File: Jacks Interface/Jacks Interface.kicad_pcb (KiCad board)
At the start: 2 copper layers, 100.6 x 33.7 mm, 11 parts, among them J1 INPUT, J10 EARTH, J11 RETURN, J2 To board GND, J3 To board IN, J4 From battery minus, J5 To board OUT, J6 OUTPUT, J7 SEND, J8 To board SEND, J9 To board RETURN

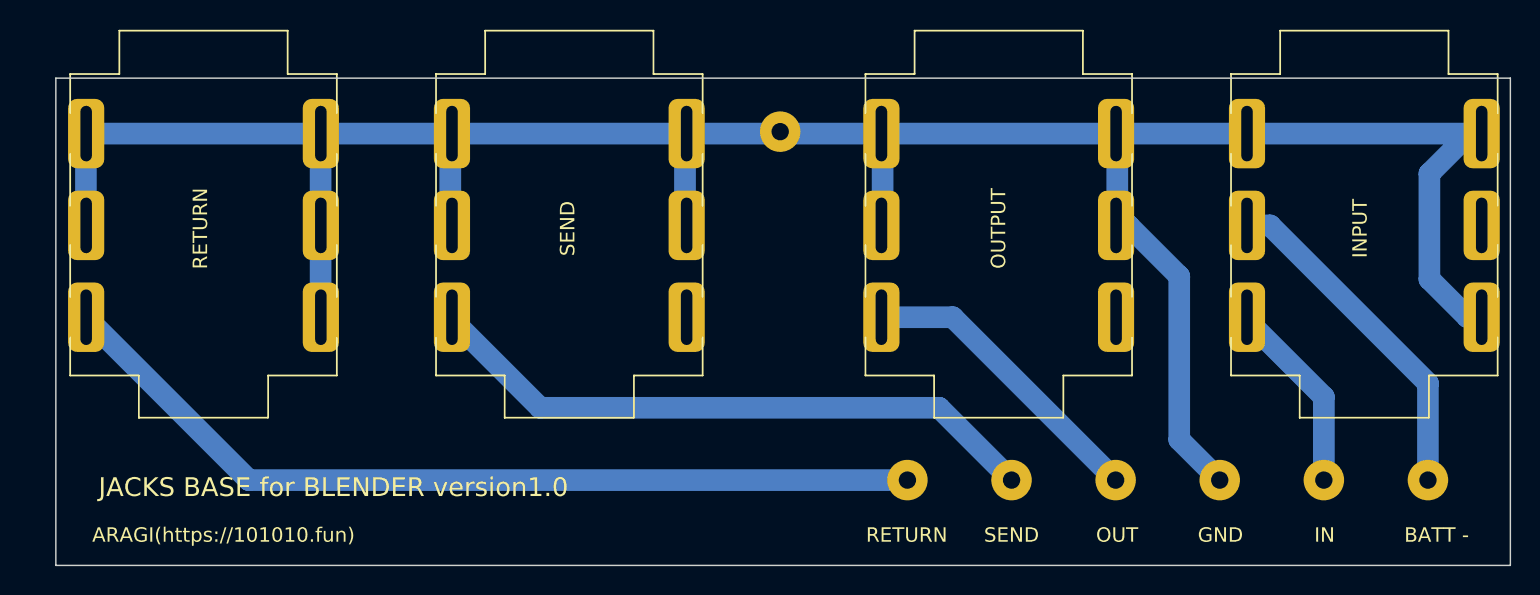
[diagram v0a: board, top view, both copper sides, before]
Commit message: fix: 回路の修正
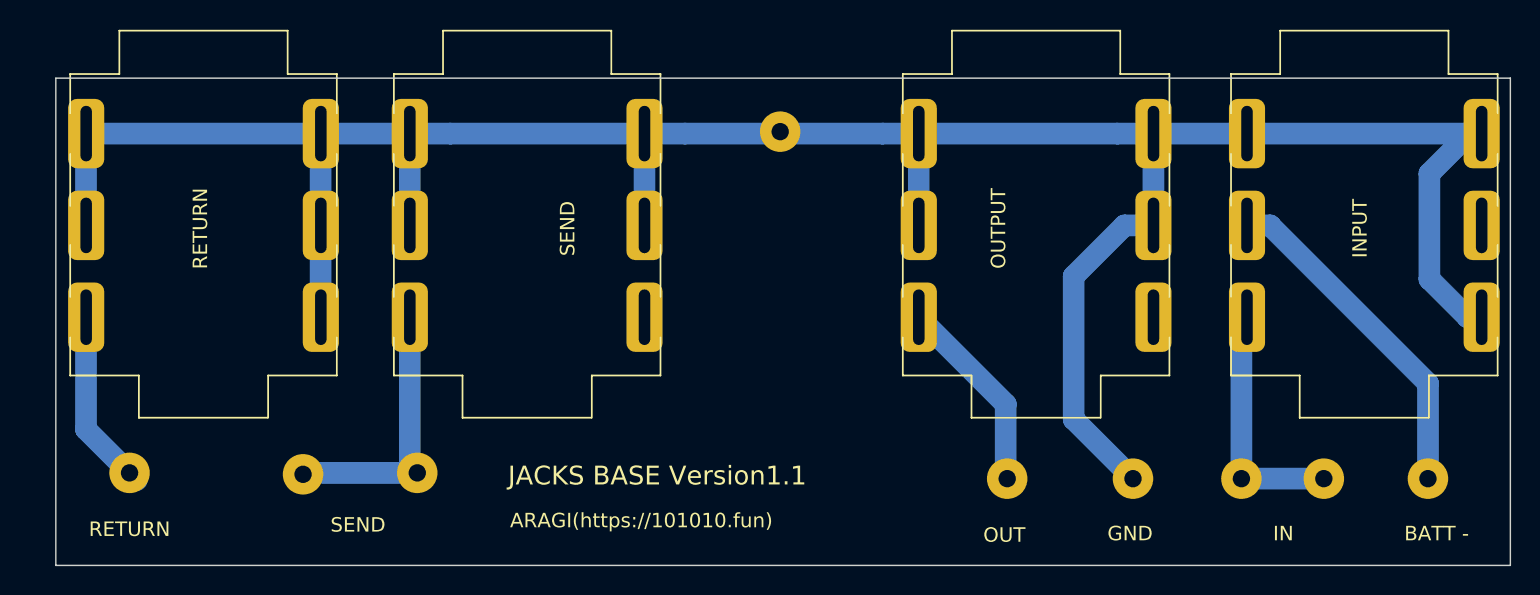
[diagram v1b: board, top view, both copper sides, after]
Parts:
- added J3: To board IN, My_Parts:Header_Pin_1p_Large, F.Cu at (144.1, 80.0)
- added J9: To board SEND, My_Parts:Header_Pin_1p_Large, F.Cu at (87.1, 79.6)
- moved J11 53.8 mm to (67.2, 79.6)
- moved J10 49.0 mm to (79.2, 79.7)
- moved J6 7.50 mm to (127.9, 80.0)
- moved J1 6.00 mm to (136.6, 80.0)
- moved J8 2.92 mm to (86.6, 68.8)
- moved J7 2.58 mm to (121.8, 68.8)
- moved J4 0.10 mm to (149.8, 80.0)
- moved J5 0.10 mm to (157.0, 80.0)
- renumbered J2 to J1, J8 to J10, J9 to J11, J11 to J12, J10 to J13, J1 to J2, J3 to J4, J4 to J5, J5 to J6, J6 to J7, J7 to J8
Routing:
- net Net-(J12-PadT): track 61.5 -> 12.7 mm
- net Net-(J8-PadT): track 43.5 -> 18.9 mm
- net Net-(J6-Pad1): track 20.8 -> 13.7 mm
- net Net-(J2-PadT): track 13.5 -> 17.1 mm
- net GND: track 178.1 -> 179.8 mm
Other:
- board text added: "JACKS BASE Version1.1"
- board text removed: "JACKS BASE for BLENDER version1.0"

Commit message: fix: jack interface修正
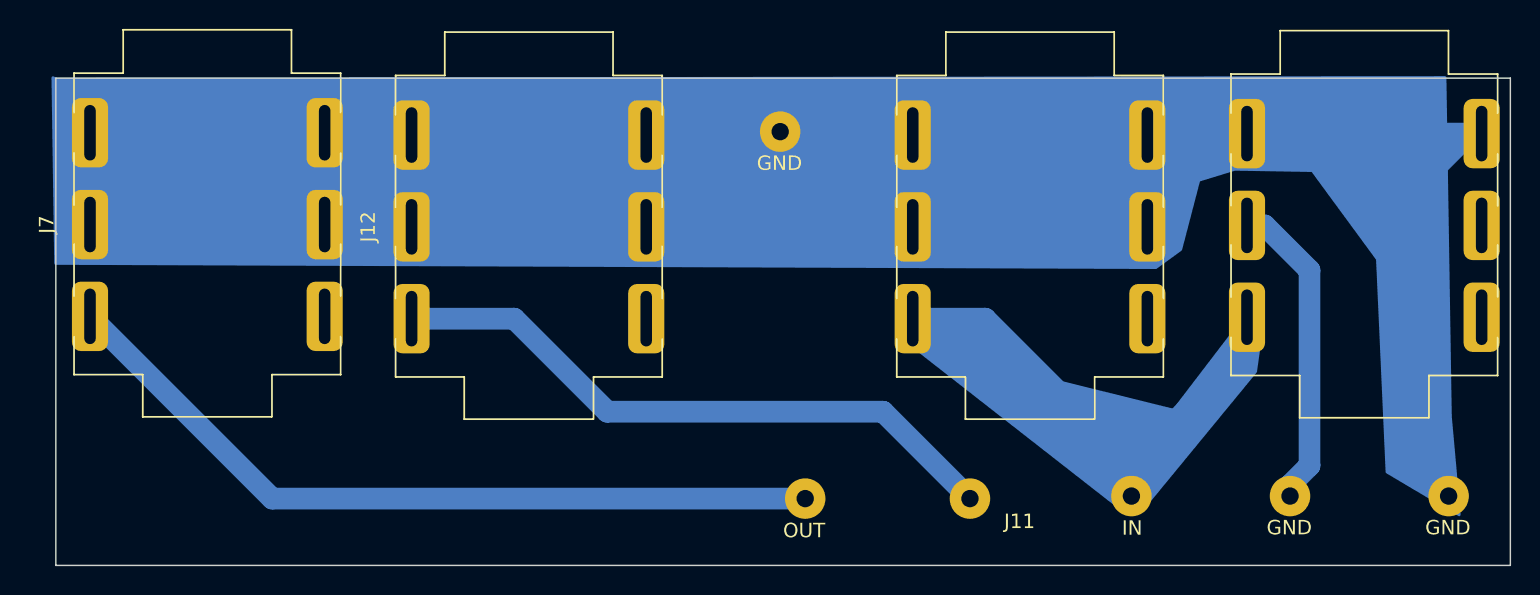
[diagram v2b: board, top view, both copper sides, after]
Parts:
- removed J10, J9: To board SEND, My_Parts:Header_Pin_1p_Large
- removed J3: To board IN, My_Parts:Header_Pin_1p_Large
- J1, J13: footprint My_Parts:Header_Pin_1p_Large -> My_Parts:Header_Pin_1p_Large_GND
- J11: value To board RETURN -> To board RETURN
- J4: footprint My_Parts:Header_Pin_1p_Large -> My_Parts:Header_Pin_1p_Large_IN
- J5: value From battery minus -> To SW GND; footprint My_Parts:Header_Pin_1p_Large -> My_Parts:Header_Pin_1p_Large_GND
- J6: footprint My_Parts:Header_Pin_1p_Large -> My_Parts:Header_Pin_1p_Large_OUT
- moved J11 58.2 mm to (125.3, 81.4)
- moved J7 57.3 mm to (64.5, 68.8)
- moved J8 34.8 mm to (121.4, 68.9)
- moved J12 22.5 mm to (86.7, 68.9)
- moved J1 21.9 mm to (158.4, 81.2)
- moved J6 14.0 mm to (113.9, 81.4)
- moved J4 13.4 mm to (136.5, 81.2)
- moved J5 9.61 mm to (147.5, 81.2)
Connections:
- J12 pad TN: GND -> unconnected-(J12-PadTN)
- J2 pad TN: GND -> unconnected-(J2-PadTN)
- J8 pad T: Net-(J8-PadT) -> Net-(J2-PadT)
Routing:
- net Net-(J6-Pad1): track 13.7 -> 54.7 mm
- net Net-(J11-Pad1): track 12.7 -> 43.8 mm
- net Net-(J8-PadT): track 18.9 -> 0.00 mm
- net Net-(J2-PadT): track 17.1 -> 35.3 mm
- net GND: track 179.8 -> 163.1 mm
- net Net-(J2-PadR): track 23.9 -> 21.8 mm
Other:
- board text removed: "ARAGI(https://101010.fun)"
- board text removed: "BATT -"
- board text removed: "GND"
- board text removed: "IN"
- board text removed: "INPUT"
- board text removed: "JACKS BASE Version1.1"
- board text removed: "OUT"
- board text removed: "OUTPUT"
- board text removed: "RETURN"
- board text removed: "SEND"
